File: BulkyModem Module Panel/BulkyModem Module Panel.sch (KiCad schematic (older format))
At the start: 16 parts, among them J1 Front Panel, M1 Mounting_Pin, M2 Mounting_Pin, M3 Mounting_Pin, M4 Mounting_Pin, SW1 MODE, SW2 POW

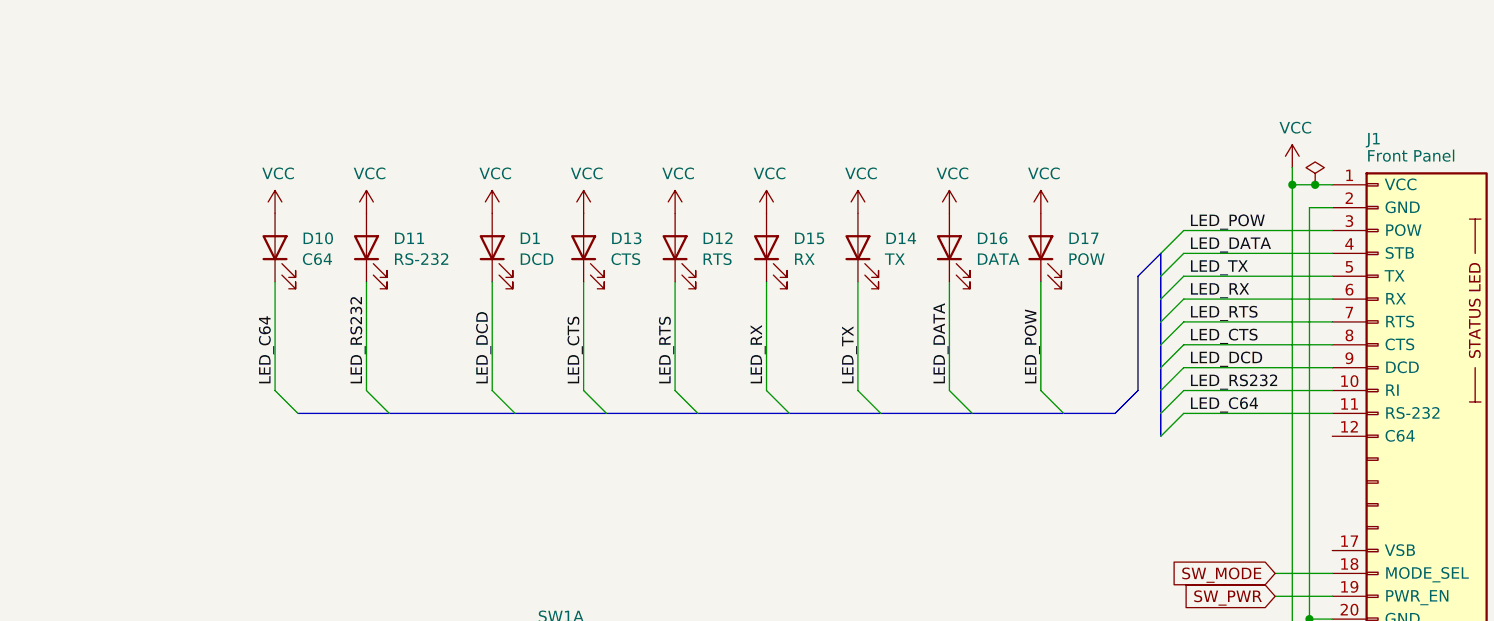
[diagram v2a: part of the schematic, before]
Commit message: Add RI LED
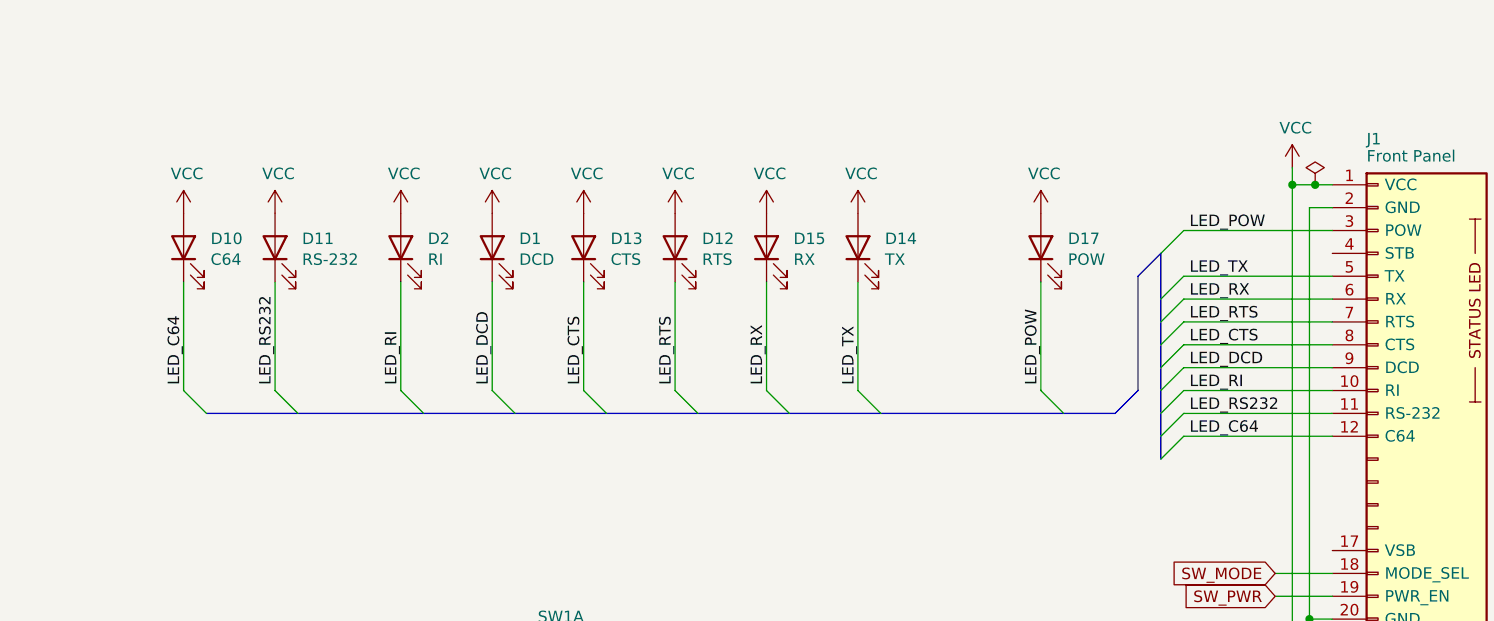
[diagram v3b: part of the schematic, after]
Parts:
- removed D16: DATA, LED_THT:LED_D5.0mm, symbol Device:LED
- added D2: RI, LED_THT:LED_D5.0mm, symbol Device:LED
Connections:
- net LED_C64: now also J1.12 (C64); no longer J1.11 (RS-232)
- net LED_RS232: now also J1.11 (RS-232); no longer J1.10 (RI)
- net VCC: now also D2.2 (A)
- net LED_DATA: no longer names the net of J1.4 (STB)
- new net LED_RI: D2.1 (K), J1.10 (RI)
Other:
- moved on the sheet: D10, D11
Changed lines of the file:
@@
 Text Label 8400 2625 0    50   ~ 0
 LED_POW
-Text Label 8400 2725 0    50   ~ 0
-LED_DATA
 Text Label 8400 2925 0    50   ~ 0
 LED_RX
@@
 Text Label 8400 3025 0    50   ~ 0
 LED_RTS
-Text Label 8400 3325 0    50   ~ 0
+Text Label 8400 3425 0    50   ~ 0
 LED_RS232
-Text Label 8400 3425 0    50   ~ 0
+Text Label 8400 3525 0    50   ~ 0
 LED_C64
 Entry Wire Line
 	8375 2625 8275 2725
 Entry Wire Line
-	8375 2725 8275 2825
-Entry Wire Line
 	8375 2825 8275 2925
 Entry Wire Line
@@
 	8375 3125 8275 3225
 Entry Wire Line
-	8375 3325 8275 3425
-Entry Wire Line
 	8375 3425 8275 3525
+Entry Wire Line
+	8375 3525 8275 3625
 $Comp
 L power:PWR_FLAG #FLG0101
@@
 	8850 4425 9025 4425
 Entry Wire Line
-	4500 3425 4400 3325
+	4100 3425 4000 3325
 $Comp
 L Device:LED D10
 U 1 1 62876713
+P 4000 2700
+F 0 "D10" V 4039 2582 50  0000 R CNN
+F 1 "C64" V 3948 2582 50  0000 R CNN
+F 2 "LED_THT:LED_D5.0mm" H 4000 2700 50  0001 C CNN
+F 3 "~" H 4000 2700 50  0001 C CNN
+	1    4000 2700
+	0    -1   -1   0
+$EndComp
+$Comp
+L power:VCC #PWR0103
+U 1 1 62876719
+P 4000 2550
+F 0 "#PWR0103" H 4000 2400 50  0001 C CNN
+F 1 "VCC" H 4015 2723 50  0000 C CNN
+F 2 "" H 4000 2550 50  0001 C CNN
+F 3 "" H 4000 2550 50  0001 C CNN
+	1    4000 2550
+	1    0    0    -1
+$EndComp
+Entry Wire Line
+	4500 3425 4400 3325
+$Comp
+L Device:LED D11
+U 1 1 62876721
 P 4400 2700
-F 0 "D10" V 4439 2582 50  0000 R CNN
-F 1 "C64" V 4348 2582 50  0000 R CNN
+F 0 "D11" V 4439 2582 50  0000 R CNN
+F 1 "RS-232" V 4348 2582 50  0000 R CNN
 F 2 "LED_THT:LED_D5.0mm" H 4400 2700 50  0001 C CNN
 F 3 "~" H 4400 2700 50  0001 C CNN
@@
 $EndComp
 $Comp
-L power:VCC #PWR0103
-U 1 1 62876719
+L power:VCC #PWR0104
+U 1 1 62876727
 P 4400 2550
-F 0 "#PWR0103" H 4400 2400 50  0001 C CNN
+F 0 "#PWR0104" H 4400 2400 50  0001 C CNN
 F 1 "VCC" H 4415 2723 50  0000 C CNN
 F 2 "" H 4400 2550 50  0001 C CNN
 F 3 "" H 4400 2550 50  0001 C CNN
 	1    4400 2550
-	1    0    0    -1
-$EndComp
-Entry Wire Line
-	4900 3425 4800 3325
-$Comp
-L Device:LED D11
-U 1 1 62876721
-P 4800 2700
-F 0 "D11" V 4839 2582 50  0000 R CNN
-F 1 "RS-232" V 4748 2582 50  0000 R CNN
-F 2 "LED_THT:LED_D5.0mm" H 4800 2700 50  0001 C CNN
-F 3 "~" H 4800 2700 50  0001 C CNN
-	1    4800 2700
-	0    -1   -1   0
-$EndComp
-$Comp
-L power:VCC #PWR0104
-U 1 1 62876727
-P 4800 2550
-F 0 "#PWR0104" H 4800 2400 50  0001 C CNN
-F 1 "VCC" H 4815 2723 50  0000 C CNN
-F 2 "" H 4800 2550 50  0001 C CNN
-F 3 "" H 4800 2550 50  0001 C CNN
-	1    4800 2550
 	1    0    0    -1
 $EndComp
@@
 $EndComp
 Entry Wire Line
-	7450 3425 7350 3325
-$Comp
-L Device:LED D16
-U 1 1 62876767
-P 7350 2700
-F 0 "D16" V 7389 2582 50  0000 R CNN
-F 1 "DATA" V 7298 2582 50  0000 R CNN
-F 2 "LED_THT:LED_D5.0mm" H 7350 2700 50  0001 C CNN
-F 3 "~" H 7350 2700 50  0001 C CNN
-	1    7350 2700
-	0    -1   -1   0
-$EndComp
-$Comp
-L power:VCC #PWR0109
-U 1 1 6287676D
-P 7350 2550
-F 0 "#PWR0109" H 7350 2400 50  0001 C CNN
-F 1 "VCC" H 7365 2723 50  0000 C CNN
-F 2 "" H 7350 2550 50  0001 C CNN
-F 3 "" H 7350 2550 50  0001 C CNN
-	1    7350 2550
-	1    0    0    -1
-$EndComp
-Entry Wire Line
 	7850 3425 7750 3325
 $Comp
@@
 	8375 2625 9025 2625
 Wire Wire Line
-	8375 2725 9025 2725
-Wire Wire Line
 	8375 2825 9025 2825
 Wire Wire Line
@@
 	8375 3125 9025 3125
 Wire Wire Line
-	8375 3325 9025 3325
-Wire Wire Line
 	8375 3425 9025 3425
+Wire Wire Line
+	8375 3525 9025 3525
 Wire Wire Line
 	8775 4125 9025 4125
@@
 Text Label 7750 3300 1    50   ~ 0
 LED_POW
-Text Label 7350 3300 1    50   ~ 0
-LED_DATA
 Text Label 6550 3300 1    50   ~ 0
 LED_RX
@@
 Text Label 6150 3300 1    50   ~ 0
 LED_RTS
-Text Label 4800 3300 1    50   ~ 0
+Text Label 4400 3300 1    50   ~ 0
 LED_RS232
-Text Label 4400 3300 1    50   ~ 0
+Text Label 4000 3300 1    50   ~ 0
 LED_C64
 Wire Wire Line
+	4000 2850 4000 3325
+Wire Wire Line
 	4400 2850 4400 3325
 Wire Wire Line
-	4800 2850 4800 3325
-Wire Wire Line
 	6150 2850 6150 3325
 Wire Wire Line
@@
 Wire Wire Line
 	6550 3325 6550 2850
-Wire Wire Line
-	7350 2850 7350 3325
 Wire Wire Line
 	7750 3325 7750 2850
@@
 Wire Wire Line
 	5350 3325 5350 2850
+Text Label 8400 3325 0    50   ~ 0
+LED_RI
+Entry Wire Line
+	8375 3325 8275 3425
+Wire Wire Line
+	8375 3325 9025 3325
+Entry Wire Line
+	5050 3425 4950 3325
+$Comp
+L Device:LED D2
+U 1 1 62E152EA
+P 4950 2700
+F 0 "D2" V 4989 2582 50  0000 R CNN
+F 1 "RI" V 4898 2582 50  0000 R CNN
+F 2 "LED_THT:LED_D5.0mm" H 4950 2700 50  0001 C CNN
+F 3 "~" H 4950 2700 50  0001 C CNN
+	1    4950 2700
+	0    -1   -1   0
+$EndComp
+$Comp
+L power:VCC #PWR0114
+U 1 1 62E152F0
+P 4950 2550
+F 0 "#PWR0114" H 4950 2400 50  0001 C CNN
+F 1 "VCC" H 4965 2723 50  0000 C CNN
+F 2 "" H 4950 2550 50  0001 C CNN
+F 3 "" H 4950 2550 50  0001 C CNN
+	1    4950 2550
+	1    0    0    -1
+$EndComp
+Text Label 4950 3300 1    50   ~ 0
+LED_RI
+Wire Wire Line
+	4950 3325 4950 2850
 Wire Bus Line
-	4500 3425 8075 3425
+	4100 3425 8075 3425
 Wire Bus Line
-	8275 2725 8275 3525
+	8275 2725 8275 3625
 $EndSCHEMATC

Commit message: Layout updated
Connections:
- no-connect marks 6 -> 8
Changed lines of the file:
@@
 Wire Wire Line
 	4950 3325 4950 2850
+NoConn ~ 9025 2725
+NoConn ~ 9025 4025
 Wire Bus Line
 	4100 3425 8075 3425

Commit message: Alternate panel designs
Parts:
- added D3, D4: 1N4148, Diode_THT:D_DO-35_SOD27_P7.62mm_Horizontal, symbol Diode:1N4148
- added JP1: BYPASS, solder_bridge:bridge, symbol Jumper:SolderJumper_2_Open
- added R1: 470, Resistor_THT:R_Axial_DIN0207_L6.3mm_D2.5mm_P10.16mm_Horizontal, symbol Device:R
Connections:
- net labels added: VSB
- wire segments 49 -> 62
- no-connect marks 8 -> 7
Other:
- note added: "Over-complicated power light,\nthe idea is that when it is on\nstandby then the LED is dimmed.\nLink JP1 and skip remaining to\nskip this questionable "feature"."
- moved on the sheet: D1, D10, D11, D12, D13, D14, D15, D17, D2, J1, SW1A, SW1B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
